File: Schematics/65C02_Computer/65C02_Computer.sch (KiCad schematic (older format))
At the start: 24 parts

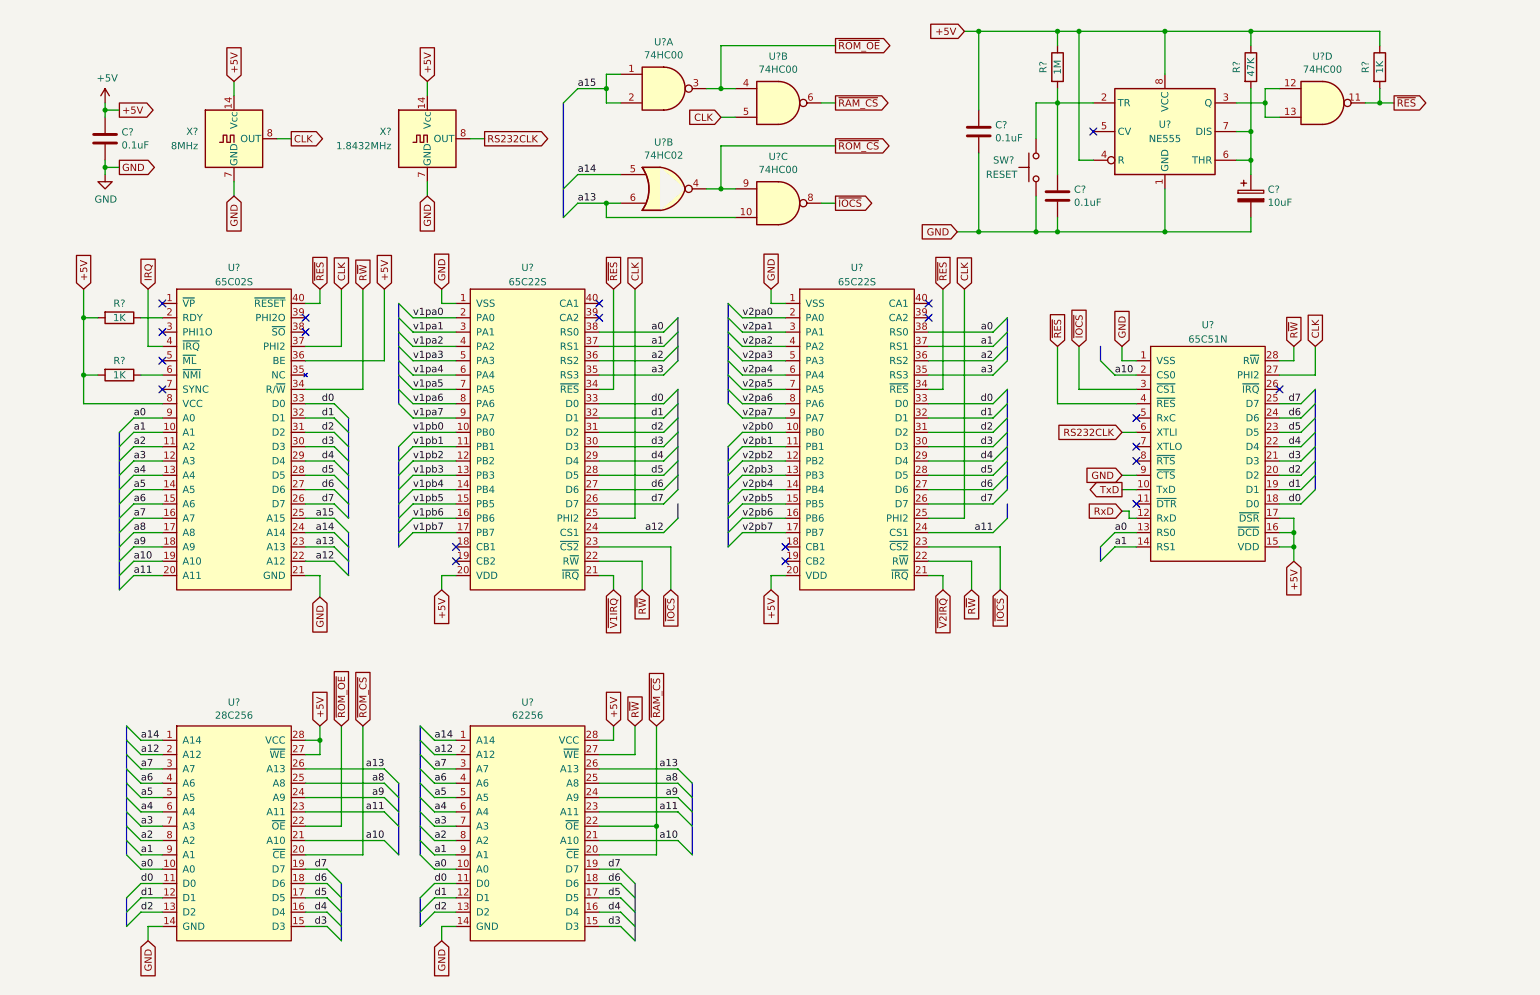
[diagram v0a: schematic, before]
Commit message: Added IRQ connections
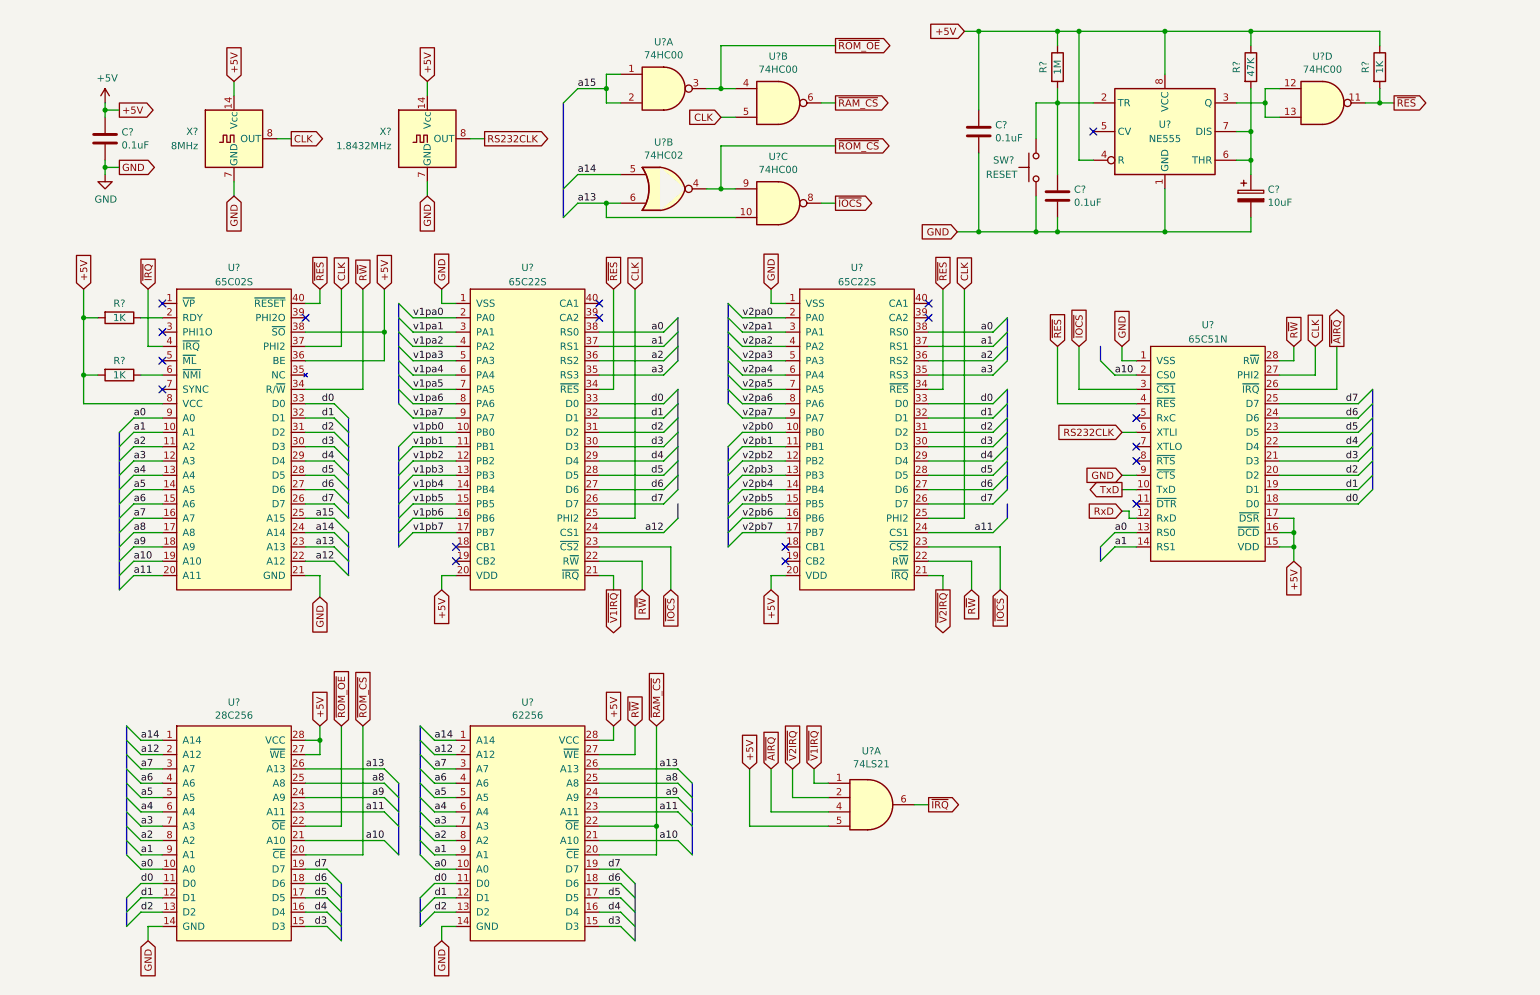
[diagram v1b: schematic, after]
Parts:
- added U?: 74LS21, Package_DIP:DIP-14_W7.62mm_Socket, symbol 74xx:74LS21
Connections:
- net +5V: now also U?.38 (~SO), U?.5
- net ~V1IRQ: now also U?.1
- net ~V2IRQ: now also U?.2
- net ~AIRQ: now reaches U?.26 (~IRQ)
- net ~AIRQ: now also U?.4
- net IRQ renamed ~IRQ
- net ~IRQ: now also U?.6
- no-connect marks 20 -> 18
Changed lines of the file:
@@
 EESchema Schematic File Version 4
-EELAYER 30 0
+LIBS:65C02_Computer-cache
+EELAYER 26 0
 EELAYER END
 $Descr A4 11693 8268
@@
 $EndDescr
 Text GLabel 1600 2500 1    50   Input ~ 0
-IRQ
+~IRQ
 Wire Wire Line
 	1600 2500 1600 2900
@@
 Wire Wire Line
 	3100 3200 2700 3200
-NoConn ~ 2700 2800
 NoConn ~ 2700 2700
 NoConn ~ 1700 3200
@@
 Entry Wire Line
 	5650 4300 5750 4200
-Text GLabel 4850 4600 3    50   Input ~ 0
+Text GLabel 4850 4600 3    50   Output ~ 0
 ~V1IRQ
-Text GLabel 7150 4600 3    50   Input ~ 0
+Text GLabel 7150 4600 3    50   Output ~ 0
 ~V2IRQ
 Wire Wire Line
@@
 	8400 3000 8500 3000
 NoConn ~ 8500 3600
-NoConn ~ 9500 3200
 NoConn ~ 8500 3700
 NoConn ~ 8500 4000
@@
 Wire Wire Line
 	9750 3100 9500 3100
-Text Label 9650 4000 2    50   ~ 0
+Text Label 10050 4000 2    50   ~ 0
 d0
-Text Label 9650 3900 2    50   ~ 0
+Text Label 10050 3900 2    50   ~ 0
 d1
-Text Label 9650 3800 2    50   ~ 0
+Text Label 10050 3800 2    50   ~ 0
 d2
-Text Label 9650 3700 2    50   ~ 0
+Text Label 10050 3700 2    50   ~ 0
 d3
-Text Label 9650 3600 2    50   ~ 0
+Text Label 10050 3600 2    50   ~ 0
 d4
-Text Label 9650 3500 2    50   ~ 0
+Text Label 10050 3500 2    50   ~ 0
 d5
-Text Label 9650 3400 2    50   ~ 0
+Text Label 10050 3400 2    50   ~ 0
 d6
-Text Label 9650 3300 2    50   ~ 0
+Text Label 10050 3300 2    50   ~ 0
 d7
 Wire Wire Line
-	9500 3300 9650 3300
-Wire Wire Line
-	9500 3400 9650 3400
-Wire Wire Line
-	9500 3500 9650 3500
-Wire Wire Line
-	9500 3600 9650 3600
-Wire Wire Line
-	9500 3700 9650 3700
-Wire Wire Line
-	9500 3800 9650 3800
-Wire Wire Line
-	9500 3900 9650 3900
-Wire Wire Line
-	9500 4000 9650 4000
-Entry Wire Line
-	9650 3300 9750 3200
-Entry Wire Line
-	9650 3400 9750 3300
-Entry Wire Line
-	9650 3500 9750 3400
-Entry Wire Line
-	9650 3600 9750 3500
-Entry Wire Line
-	9650 3700 9750 3600
-Entry Wire Line
-	9650 3800 9750 3700
-Entry Wire Line
-	9650 3900 9750 3800
-Entry Wire Line
-	9650 4000 9750 3900
+	9500 3300 10050 3300
+Wire Wire Line
+	9500 3400 10050 3400
+Wire Wire Line
+	9500 3500 10050 3500
+Wire Wire Line
+	9500 3600 10050 3600
+Wire Wire Line
+	9500 3700 10050 3700
+Wire Wire Line
+	9500 3800 10050 3800
+Wire Wire Line
+	9500 3900 10050 3900
+Wire Wire Line
+	9500 4000 10050 4000
+Entry Wire Line
+	10050 3300 10150 3200
+Entry Wire Line
+	10050 3400 10150 3300
+Entry Wire Line
+	10050 3500 10150 3400
+Entry Wire Line
+	10050 3600 10150 3500
+Entry Wire Line
+	10050 3700 10150 3600
+Entry Wire Line
+	10050 3800 10150 3700
+Entry Wire Line
+	10050 3900 10150 3800
+Entry Wire Line
+	10050 4000 10150 3900
 Text Label 8350 3100 0    50   ~ 0
 a10
@@
 	2700 3000 3250 3000
 Wire Wire Line
-	3250 3000 3250 2500
+	3250 3000 3250 2800
 $Comp
 L 74xx:74HC00 U?
@@
 Wire Wire Line
 	4800 2000 5700 2000
+Connection ~ 4800 1900
+Wire Wire Line
+	4800 1900 4600 1900
+$Comp
+L 74xx:74LS21 U?
+U 1 1 5E23A6D1
+P 6650 6100
+F 0 "U?" H 6650 6475 50  0000 C CNN
+F 1 "74LS21" H 6650 6384 50  0000 C CNN
+F 2 "Package_DIP:DIP-14_W7.62mm_Socket" H 6650 6100 50  0001 C CNN
+F 3 "http://www.ti.com/lit/gpn/sn74LS21" H 6650 6100 50  0001 C CNN
+	1    6650 6100
+	1    0    0    -1
+$EndComp
+Text GLabel 9900 2900 1    50   Output ~ 0
+~AIRQ
+Wire Wire Line
+	9500 3200 9900 3200
+Wire Wire Line
+	9900 3200 9900 2900
+Text GLabel 6250 5850 1    50   Input ~ 0
+~V1IRQ
+Text GLabel 6100 5850 1    50   Input ~ 0
+~V2IRQ
+Text GLabel 5950 5850 1    50   Input ~ 0
+~AIRQ
+Text GLabel 5800 5850 1    50   Input ~ 0
++5V
+Wire Wire Line
+	6250 5850 6250 5950
+Wire Wire Line
+	6250 5950 6350 5950
+Wire Wire Line
+	6100 5850 6100 6050
+Wire Wire Line
+	6100 6050 6350 6050
+Wire Wire Line
+	5950 5850 5950 6150
+Wire Wire Line
+	5950 6150 6350 6150
+Wire Wire Line
+	5800 5850 5800 6250
+Wire Wire Line
+	5800 6250 6350 6250
+Text GLabel 7050 6100 2    50   Output ~ 0
+~IRQ
+Wire Wire Line
+	6950 6100 7050 6100
+Wire Wire Line
+	2700 2800 3250 2800
 Wire Bus Line
 	3500 6750 3500 6950
@@
 	5650 3600 5650 4300
 Wire Bus Line
-	9750 3200 9750 3900
+	10150 3200 10150 3900
 Wire Bus Line
 	3500 5550 3500 6450
@@
 Wire Bus Line
 	1400 3500 1400 4600
-Connection ~ 4800 1900
-Wire Wire Line
-	4800 1900 4600 1900
+Connection ~ 3250 2800
+Wire Wire Line
+	3250 2800 3250 2500
 $EndSCHEMATC

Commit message: Added bypass caps, moved things around
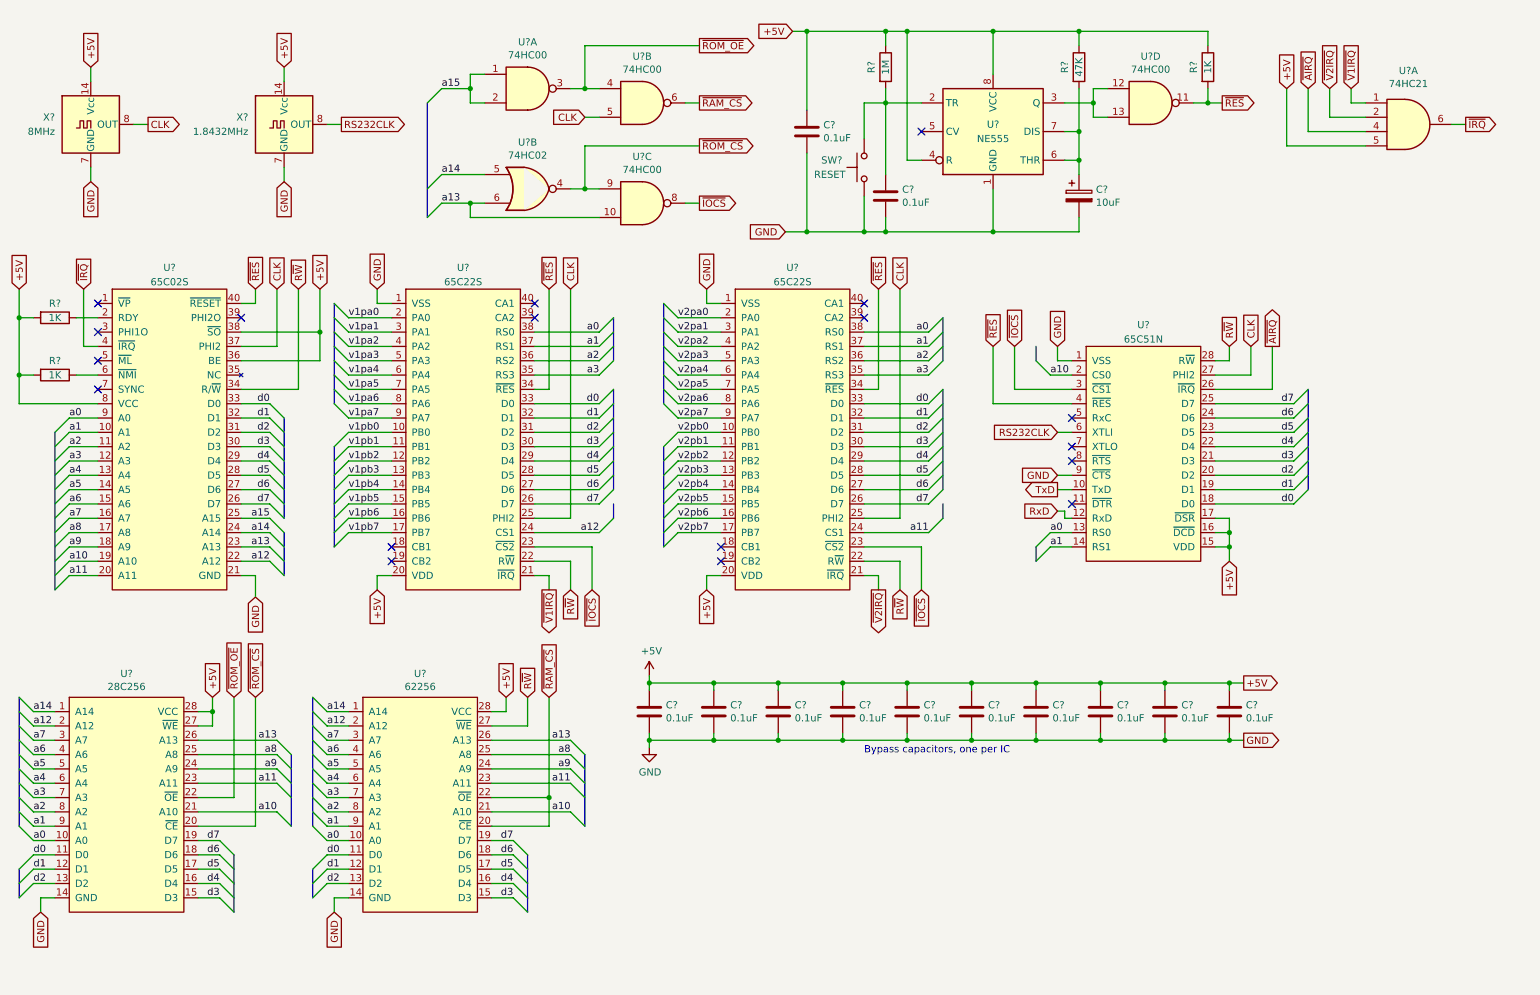
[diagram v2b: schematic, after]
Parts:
- added C? (x9): 0.1uF, Capacitor_THT:C_Disc_D3.4mm_W2.1mm_P2.50mm, symbol Device:C
- U?: value 74LS21 -> 74HC21
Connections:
- net +5V: now also C?.1, C?.1, C?.1, C?.1, C?.1, C?.1, C?.1, C?.1, C?.1
- net GND: now also C?.2, C?.2, C?.2, C?.2, C?.2, C?.2, C?.2, C?.2, C?.2
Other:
- note added: "Bypass capacitors, one per IC"
- moved on the sheet: C?, R?, SW?, U?, U?A, U?B, U?C, U?D, X?

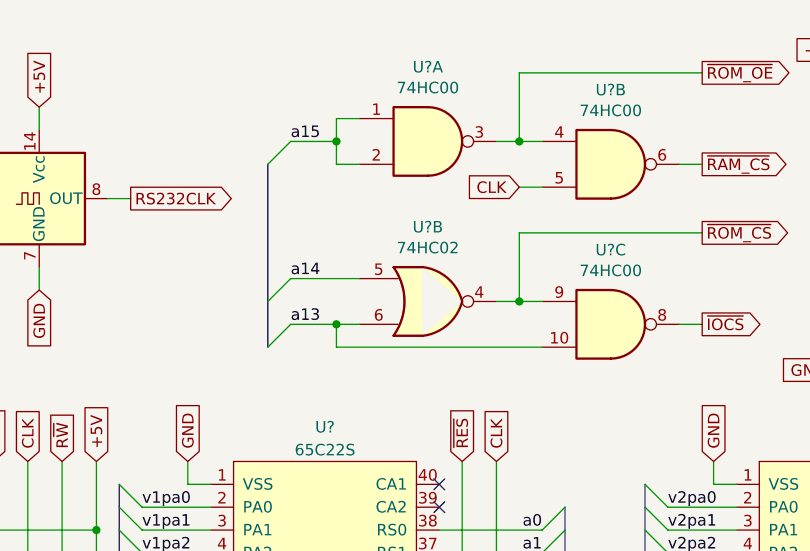
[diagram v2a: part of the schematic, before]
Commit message: Fixed address decoder bug
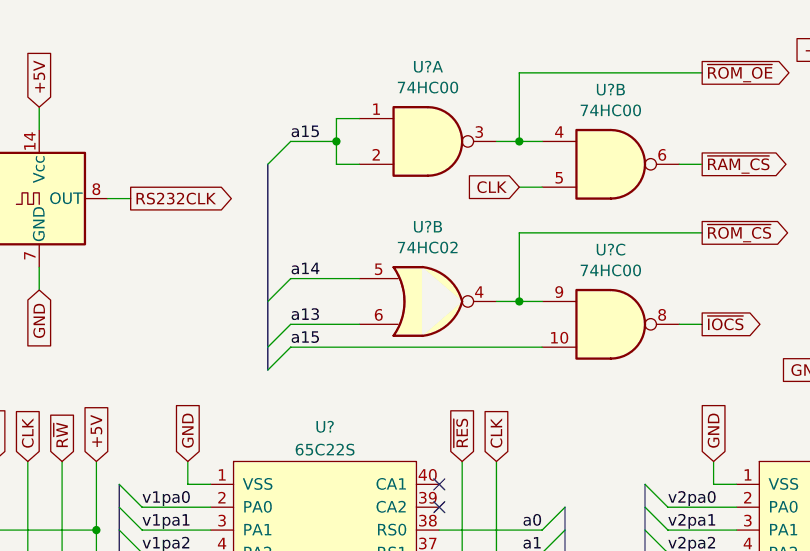
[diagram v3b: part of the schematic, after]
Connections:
- net a13: no longer U?.10
- net a15: now also U?.10
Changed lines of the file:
@@
 a13
-Wire Wire Line
-	3950 1900 3850 1900
 Wire Wire Line
 	3950 1700 3650 1700
@@
 Wire Wire Line
 	8200 1200 8200 1300
-Wire Wire Line
-	3850 1900 3850 2000
-Wire Wire Line
-	3850 2000 4750 2000
-Connection ~ 3850 1900
-Wire Wire Line
-	3850 1900 3650 1900
 $Comp
 L 74xx:74LS21 U?
@@
 	5100 5650 5100 5700
 Connection ~ 5100 5650
-Wire Bus Line
-	2750 6550 2750 6750
-Wire Bus Line
-	700  6550 700  6750
-Wire Bus Line
-	3550 1200 3550 2000
-Wire Bus Line
-	2550 4200 2550 4500
-Wire Bus Line
-	4850 2700 4850 3000
-Wire Bus Line
-	7150 2700 7150 3000
-Wire Bus Line
-	4650 5750 4650 6250
-Wire Bus Line
-	4250 6450 4250 6850
-Wire Bus Line
-	2600 5750 2600 6250
-Wire Bus Line
-	2200 6450 2200 6850
-Wire Bus Line
-	2550 3400 2550 4100
-Wire Bus Line
-	4850 3200 4850 3900
-Wire Bus Line
-	7150 3200 7150 3900
-Wire Bus Line
-	2900 2600 2900 3300
-Wire Bus Line
-	2900 3600 2900 4300
-Wire Bus Line
-	5200 2600 5200 3300
-Wire Bus Line
-	5200 3600 5200 4300
-Wire Bus Line
-	9700 3200 9700 3900
-Wire Bus Line
-	2750 5350 2750 6250
-Wire Bus Line
-	700  5350 700  6250
-Wire Bus Line
-	950  3500 950  4600
 Text Notes 6600 5750 0    50   ~ 0
 Bypass capacitors, one per IC
+Entry Wire Line
+	3550 2100 3650 2000
+Wire Wire Line
+	3650 1900 3950 1900
+Wire Wire Line
+	3650 2000 4750 2000
+Wire Bus Line
+	2750 6550 2750 6750
+Wire Bus Line
+	700  6550 700  6750
+Wire Bus Line
+	2550 4200 2550 4500
+Wire Bus Line
+	4850 2700 4850 3000
+Wire Bus Line
+	7150 2700 7150 3000
+Wire Bus Line
+	3550 1200 3550 2100
+Wire Bus Line
+	4650 5750 4650 6250
+Wire Bus Line
+	4250 6450 4250 6850
+Wire Bus Line
+	2600 5750 2600 6250
+Wire Bus Line
+	2200 6450 2200 6850
+Wire Bus Line
+	2550 3400 2550 4100
+Wire Bus Line
+	4850 3200 4850 3900
+Wire Bus Line
+	7150 3200 7150 3900
+Wire Bus Line
+	2900 2600 2900 3300
+Wire Bus Line
+	2900 3600 2900 4300
+Wire Bus Line
+	5200 2600 5200 3300
+Wire Bus Line
+	5200 3600 5200 4300
+Wire Bus Line
+	9700 3200 9700 3900
+Wire Bus Line
+	2750 5350 2750 6250
+Wire Bus Line
+	700  5350 700  6250
+Wire Bus Line
+	950  3500 950  4600
+Text Label 3650 2000 0    50   ~ 0
+a15
 $EndSCHEMATC
